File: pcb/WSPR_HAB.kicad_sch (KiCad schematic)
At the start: 23 parts, among them J1 DC in, J2 Si5351, J3 LPF_input, J4 LPF_output, J5 EFHW_PRI, J6 EFHW_GND, J7 ANT_OUT, J8 ANT_GND, J9 EFHW_SEC, U1 5186, U2 7400

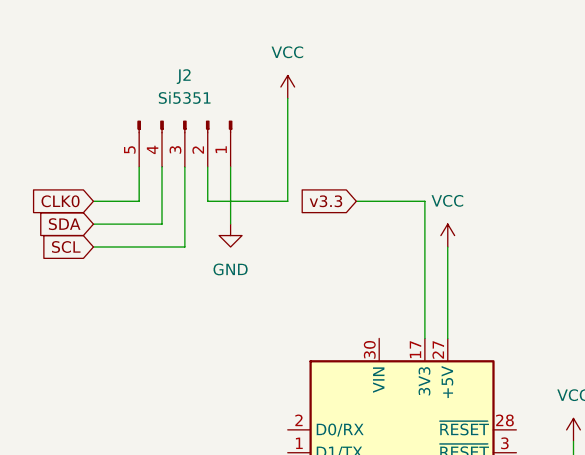
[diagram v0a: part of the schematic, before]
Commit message: added the Si5351 to the PCB
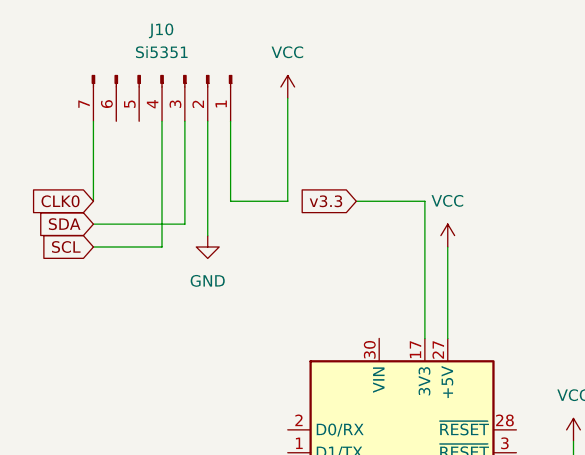
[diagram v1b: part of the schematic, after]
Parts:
- removed J2: Si5351, Connector_PinHeader_2.54mm:PinHeader_1x05_P2.54mm_Vertical, symbol Connector:Conn_01x05_Pin
- added J10: Si5351, Connector_PinHeader_2.54mm:PinHeader_1x07_P2.54mm_Vertical, symbol Connector:Conn_01x07_Pin
- R2, R3: footprint Resistor_SMD:R_0805_2012Metric -> Resistor_THT:R_Axial_DIN0204_L3.6mm_D1.6mm_P7.62mm_Horizontal
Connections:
- net CLK0: now also J10.7 (Pin_7)
- net GND: now also J10.2 (Pin_2)
- net SCL: now also J10.4 (Pin_4)
- net SDA: now also J10.3 (Pin_3)
- net VCC: now also J10.1 (Pin_1)
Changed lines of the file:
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@@
 	(wire
 		(pts
+			(xy 39.37 26.67) (xy 39.37 39.37)
+		)
+		(stroke
+			(width 0)
+			(type default)
+		)
+	)
+	(wire
+		(pts
 			(xy 73.66 76.2) (xy 78.74 76.2)
 		)
@@
 	(wire
 		(pts
-			(xy 26.67 35.56) (xy 31.75 35.56)
-		)
-		(stroke
-			(width 0)
-			(type default)
-		)
-	)
-	(wire
-		(pts
 			(xy 38.1 130.81) (xy 40.64 130.81)
 		)
@@
 	(wire
 		(pts
+			(xy 26.67 38.1) (xy 36.83 38.1)
+		)
+		(stroke
+			(width 0)
+			(type default)
+		)
+	)
+	(wire
+		(pts
 			(xy 106.68 133.35) (xy 110.49 133.35)
 		)
@@
 	(wire
 		(pts
+			(xy 34.29 40.64) (xy 26.67 40.64)
+		)
+		(stroke
+			(width 0)
+			(type default)
+		)
+	)
+	(wire
+		(pts
 			(xy 63.5 50.8) (xy 63.5 35.56)
 		)
@@
 	(wire
 		(pts
-			(xy 34.29 31.75) (xy 34.29 38.1)
+			(xy 36.83 26.67) (xy 36.83 38.1)
 		)
 		(stroke
@@
 	(wire
 		(pts
+			(xy 26.67 26.67) (xy 26.67 35.56)
+		)
+		(stroke
+			(width 0)
+			(type default)
+		)
+	)
+	(wire
+		(pts
 			(xy 133.35 68.58) (xy 129.54 68.58)
 		)
@@
 	(wire
 		(pts
-			(xy 41.91 31.75) (xy 41.91 38.1)
-		)
-		(stroke
-			(width 0)
-			(type default)
-		)
-	)
-	(wire
-		(pts
 			(xy 173.99 68.58) (xy 173.99 71.12)
 		)
@@
 	(wire
 		(pts
-			(xy 26.67 38.1) (xy 34.29 38.1)
-		)
-		(stroke
-			(width 0)
-			(type default)
-		)
-	)
-	(wire
-		(pts
 			(xy 129.54 63.5) (xy 129.54 66.04)
 		)
@@
 	(wire
 		(pts
-			(xy 39.37 35.56) (xy 48.26 35.56)
+			(xy 41.91 35.56) (xy 48.26 35.56)
 		)
 		(stroke
@@
 	(wire
 		(pts
-			(xy 36.83 31.75) (xy 36.83 40.64)
+			(xy 34.29 26.67) (xy 34.29 40.64)
 		)
 		(stroke
@@
 	(wire
 		(pts
-			(xy 31.75 31.75) (xy 31.75 35.56)
-		)
-		(stroke
-			(width 0)
-			(type default)
-		)
-	)
-	(wire
-		(pts
 			(xy 62.23 104.14) (xy 62.23 107.95)
 		)
@@
 	(wire
 		(pts
-			(xy 26.67 40.64) (xy 36.83 40.64)
-		)
-		(stroke
-			(width 0)
-			(type default)
-		)
-	)
-	(wire
-		(pts
 			(xy 213.36 48.26) (xy 213.36 49.53)
 		)
@@
 	(wire
 		(pts
-			(xy 39.37 31.75) (xy 39.37 35.56)
+			(xy 41.91 26.67) (xy 41.91 35.56)
 		)
 		(stroke
@@
 	)
 	(symbol
+		(lib_id "Connector:Conn_01x07_Pin")
+		(at 34.29 21.59 270)
+		(unit 1)
+		(exclude_from_sim no)
+		(in_bom yes)
+		(on_board yes)
+		(dnp no)
+		(fields_autoplaced yes)
+		(property "Reference" "J10"
+			(at 34.29 16.51 90)
+			(effects
+				(font
+					(size 1.27 1.27)
+				)
+			)
+		)
+		(property "Value" "Si5351"
+			(at 34.29 19.05 90)
+			(effects
+				(font
+					(size 1.27 1.27)
+				)
+			)
+		)
+		(property "Footprint" "Connector_PinHeader_2.54mm:PinHeader_1x07_P2.54mm_Vertical"
+			(at 34.29 21.59 0)
+			(effects
+				(font
+					(size 1.27 1.27)
+				)
+				(hide yes)
+			)
+		)
+		(property "Datasheet" "~"
+			(at 34.29 21.59 0)
+			(effects
+				(font
+					(size 1.27 1.27)
+				)
+				(hide yes)
+			)
+		)
+		(property "Description" "Generic connector, single row, 01x07, script generated"
+			(at 34.29 21.59 0)
+			(effects
+				(font
+					(size 1.27 1.27)
+				)
+				(hide yes)
+			)
+		)
+		(pin "4"
+		)
+		(pin "3"
+		)
+		(pin "2"
+		)
+		(pin "1"
+		)
+		(pin "5"
+		)
+		(pin "6"
+		)
+		(pin "7"
+		)
+		(instances
+			(project ""
+				(path "/8d5a18b9-9441-449d-b564-e55d8123e704"
+					(reference "J10")
+					(unit 1)
+				)
+			)
+		)
+	)
+	(symbol
 		(lib_id "Device:R")
 		(at 130.81 107.95 0)
@@
 			)
 		)
-		(property "Footprint" "Resistor_SMD:R_0805_2012Metric"
+		(property "Footprint" "Resistor_THT:R_Axial_DIN0204_L3.6mm_D1.6mm_P7.62mm_Horizontal"
 			(at 129.032 107.95 90)
 			(effects
@@
 	(symbol
 		(lib_id "power:GND")
-		(at 41.91 38.1 0)
+		(at 39.37 39.37 0)
 		(unit 1)
 		(exclude_from_sim no)
@@
 		(fields_autoplaced yes)
 		(property "Reference" "#PWR04"
-			(at 41.91 44.45 0)
+			(at 39.37 45.72 0)
 			(effects
 				(font
@@
 		)
 		(property "Value" "GND"
-			(at 41.91 43.18 0)
+			(at 39.37 44.45 0)
 			(effects
 				(font
@@
 		)
 		(property "Footprint" ""
-			(at 41.91 38.1 0)
+			(at 39.37 39.37 0)
 			(effects
 				(font
@@
 		)
 		(property "Datasheet" ""
-			(at 41.91 38.1 0)
+			(at 39.37 39.37 0)
 			(effects
 				(font
@@
 		)
 		(property "Description" "Power symbol creates a global label with name \"GND\" , ground"
-			(at 41.91 38.1 0)
+			(at 39.37 39.37 0)
 			(effects
 				(font
@@
 	)
 	(symbol
-		(lib_id "Connector:Conn_01x05_Pin")
-		(at 36.83 26.67 270)
-		(unit 1)
-		(exclude_from_sim no)
-		(in_bom yes)
-		(on_board yes)
-		(dnp no)
-		(fields_autoplaced yes)
-		(property "Reference" "J2"
-			(at 36.83 21.59 90)
-			(effects
-				(font
-					(size 1.27 1.27)
-				)
-			)
-		)
-		(property "Value" "Si5351"
-			(at 36.83 24.13 90)
-			(effects
-				(font
-					(size 1.27 1.27)
-				)
-			)
-		)
-		(property "Footprint" "Connector_PinHeader_2.54mm:PinHeader_1x05_P2.54mm_Vertical"
-			(at 36.83 26.67 0)
-			(effects
-				(font
-					(size 1.27 1.27)
-				)
-				(hide yes)
-			)
-		)
-		(property "Datasheet" "~"
-			(at 36.83 26.67 0)
-			(effects
-				(font
-					(size 1.27 1.27)
-				)
-				(hide yes)
-			)
-		)
-		(property "Description" "Generic connector, single row, 01x05, script generated"
-			(at 36.83 26.67 0)
-			(effects
-				(font
-					(size 1.27 1.27)
-				)
-				(hide yes)
-			)
-		)
-		(pin "5"
-		)
-		(pin "3"
-		)
-		(pin "2"
-		)
-		(pin "4"
-		)
-		(pin "1"
-		)
-		(instances
-			(project ""
-				(path "/8d5a18b9-9441-449d-b564-e55d8123e704"
-					(reference "J2")
-					(unit 1)
-				)
-			)
-		)
-	)
-	(symbol
 		(lib_id "Device:R")
 		(at 130.81 119.38 0)
@@
 			)
 		)
-		(property "Footprint" "Resistor_SMD:R_0805_2012Metric"
+		(property "Footprint" "Resistor_THT:R_Axial_DIN0204_L3.6mm_D1.6mm_P7.62mm_Horizontal"
 			(at 129.032 119.38 90)
 			(effects

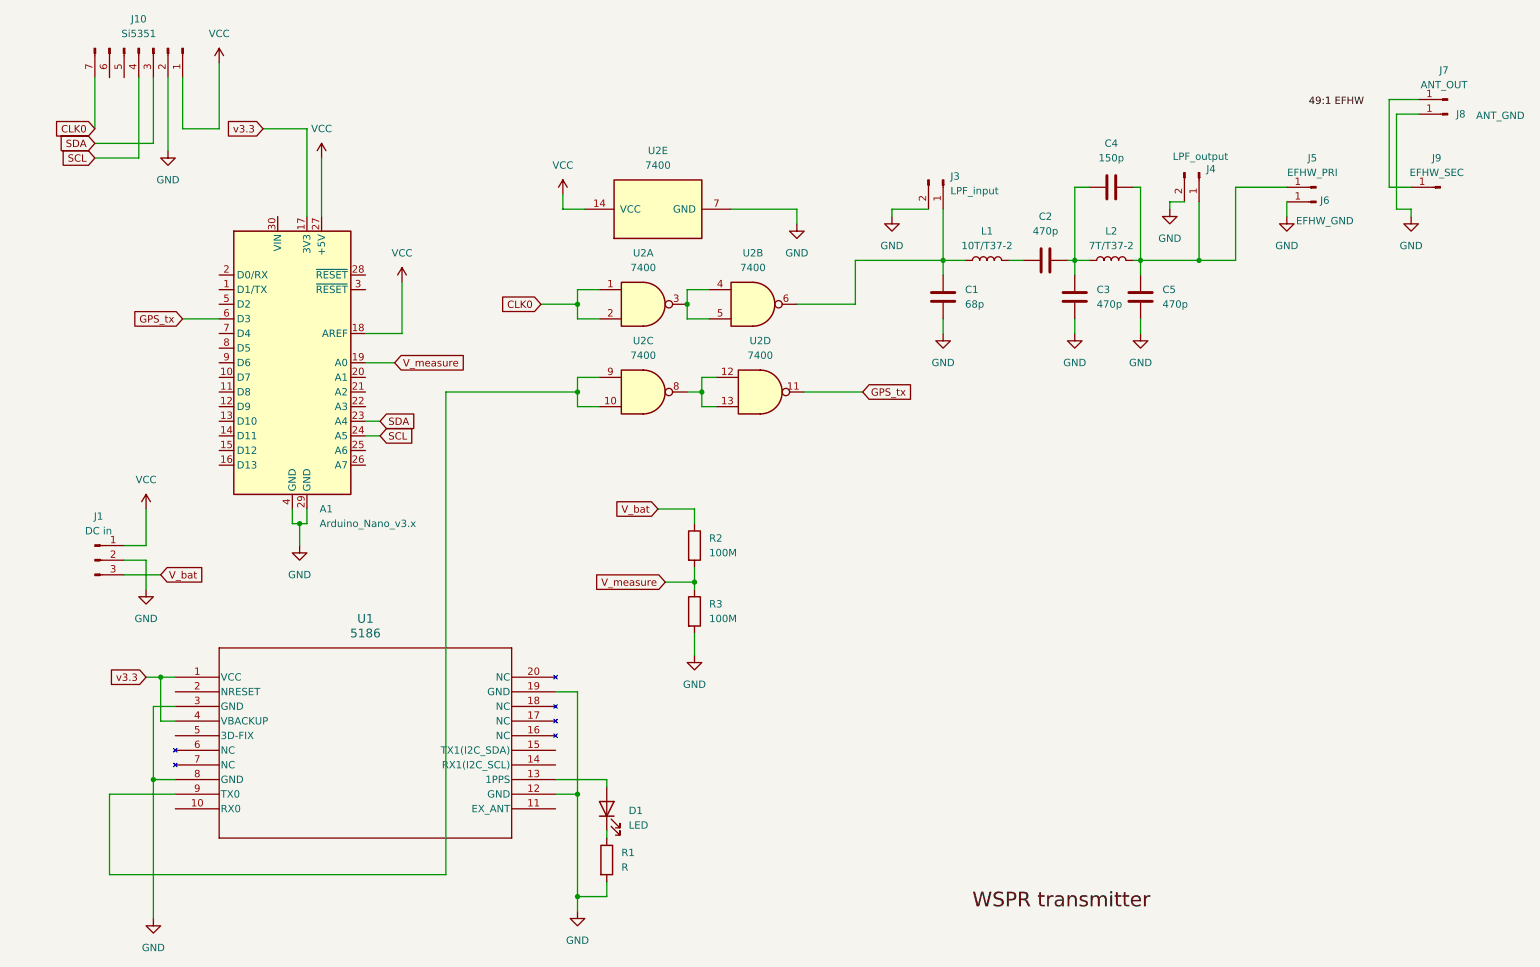
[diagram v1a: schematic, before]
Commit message: added a mosfet and extra pins to the gps
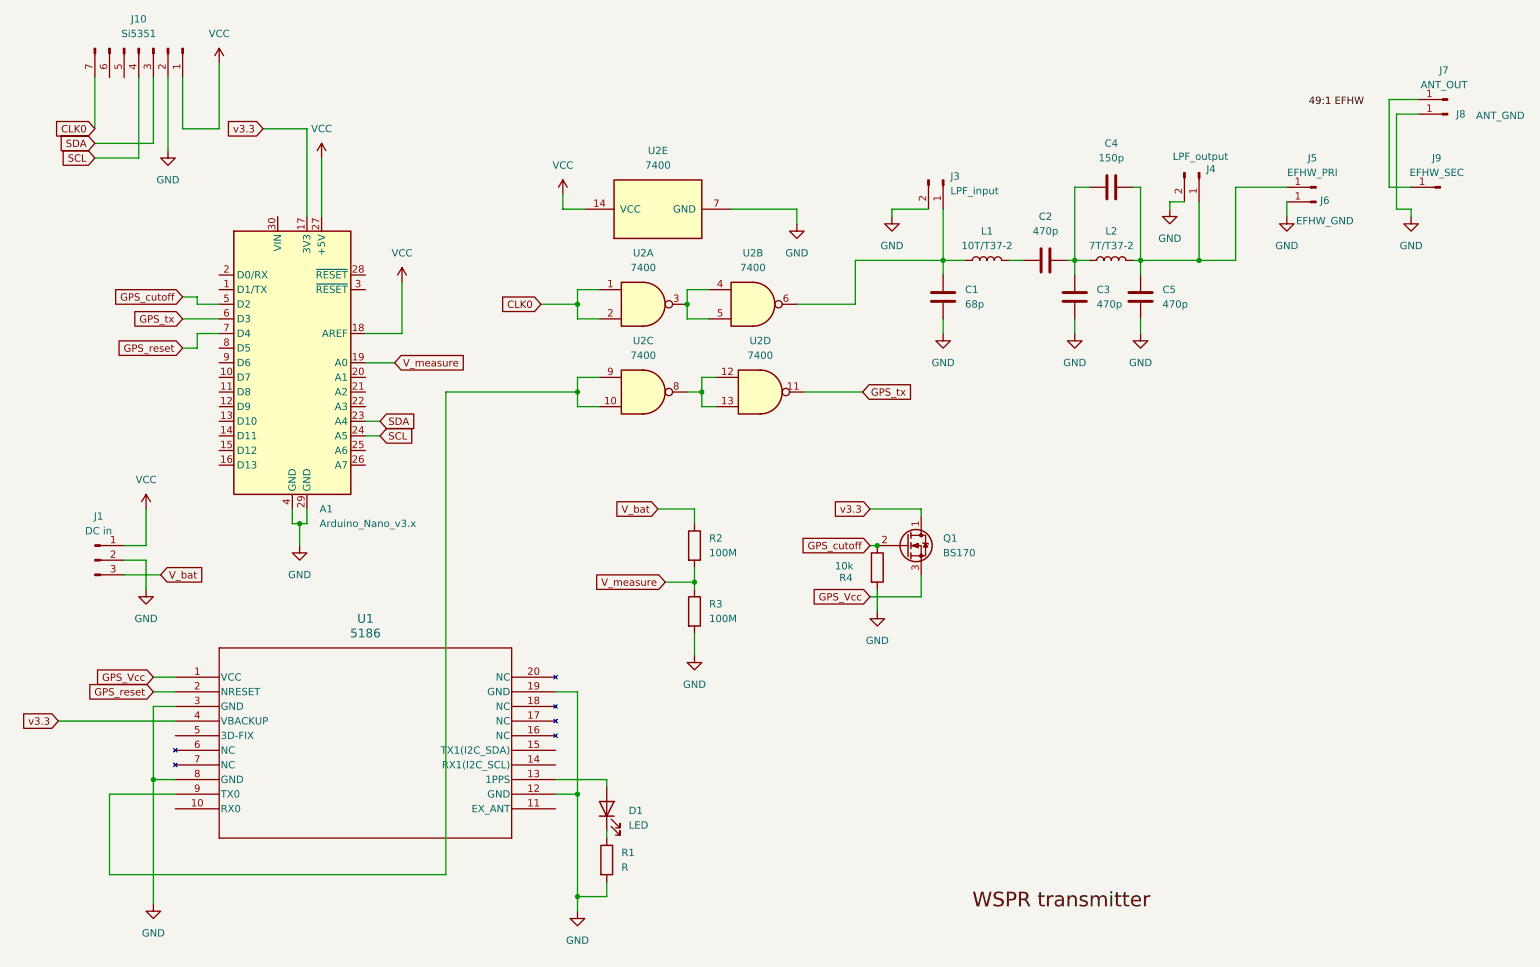
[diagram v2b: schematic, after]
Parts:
- added Q1: BS170, Package_TO_SOT_THT:TO-92_Inline, symbol Transistor_FET:BS170
- added R4: 10k, Resistor_THT:R_Axial_DIN0204_L3.6mm_D1.6mm_P7.62mm_Horizontal, symbol Device:R
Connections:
- net GND: now also R4.2
- net v3.3: now also Q1.1 (D); no longer U1.1 (VCC)
- net GPS_cutoff: now reaches A1.5 (D2)
- net GPS_cutoff: now also Q1.2 (G), R4.1
- net GPS_reset: now reaches A1.7 (D4)
- net GPS_reset: now also U1.2 (NRESET)
- new net GPS_Vcc: Q1.3 (S), U1.1 (VCC)
